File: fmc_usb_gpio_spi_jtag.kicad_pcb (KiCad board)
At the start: 2 copper layers, 76.5 x 69 mm, 146 parts, among them J1 SAMTEC_ASP-134604-01, J2 ACA-SPI-004-K02, J3 USB_C_Receptacle, J4 USB_C_Receptacle, J5 Conn_JTAG_20, J6 PM2.54-2x6, J7 Micro_SD_Card_Det2, J8 PM2.54-2x6, SW1 DSHP04TSGET, SW10 TL3342F160QG, SW2 TL3342F160QG, SW7 TL3342F160QG, SW8 TL3342F160QG, SW9 TL3342F160QG, U1 M24C02-FMN, U11 TXS02612RTWR, U12 TPD4E02B04DQA, U13 MT2492, U14 TXS02612RTWR, U15 TXS02612RTWR, U16 TXS02612RTWR, U17 TXS02612RTWR, U18 TPD4E02B04DQA, U19 TPD4E02B04DQA, U2 STUSB03EQR, U20 TPD4E02B04DQA, U21 AIP74LVC1T45GB236TR, U22 AIP74LVC1T45GB236TR, U23 AIP74LVC1T45GB236TR, U24 AIP74LVC1T45GB236TR, U25 MMC5603NJ, U26 TXS02612RTWR, U27 TXS02612RTWR, U3 CP2104, U4 TXS02612RTWR, U5 GX0011D

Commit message: *.*: add design rule file of PCB
Signed-off-by: Huang Rui <vowstar@gmail.com>
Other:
- copper layers 2 -> 4
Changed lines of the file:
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@@
   (layers
     (0 "F.Cu" signal)
+    (1 "In1.Cu" signal)
+    (2 "In2.Cu" signal)
     (31 "B.Cu" signal)
     (32 "B.Adhes" user "B.Adhesive")
@@
   )
   (setup
+    (stackup
+      (layer "F.SilkS" (type "Top Silk Screen"))
+      (layer "F.Paste" (type "Top Solder Paste"))
+      (layer "F.Mask" (type "Top Solder Mask") (thickness 0.01))
+      (layer "F.Cu" (type "copper") (thickness 0.035))
+      (layer "dielectric 1" (type "prepreg") (thickness 0.1) (material "FR4") (epsilon_r 4.5) (loss_tangent 0.02))
+      (layer "In1.Cu" (type "copper") (thickness 0.035))
+      (layer "dielectric 2" (type "core") (thickness 1.24) (material "FR4") (epsilon_r 4.5) (loss_tangent 0.02))
+      (layer "In2.Cu" (type "copper") (thickness 0.035))
+      (layer "dielectric 3" (type "prepreg") (thickness 0.1) (material "FR4") (epsilon_r 4.5) (loss_tangent 0.02))
+      (layer "B.Cu" (type "copper") (thickness 0.035))
+      (layer "B.Mask" (type "Bottom Solder Mask") (thickness 0.01))
+      (layer "B.Paste" (type "Bottom Solder Paste"))
+      (layer "B.SilkS" (type "Bottom Silk Screen"))
+      (copper_finish "None")
+      (dielectric_constraints no)
+    )
     (pad_to_mask_clearance 0)
     (aux_axis_origin 114.343703 64.989968)
@@
     (fp_arc (start 3.8 2.46) (mid 3.860908 2.157784) (end 4.03 1.9)
       (stroke (width 0.127) (type default)) (layer "F.SilkS"))
-    (fp_arc (start 4.03 -1.9) (mid 3.860909 -2.157783) (end 3.8 -2.46)
+    (fp_arc (start 4.03 -1.9) (mid 3.860928 -2.157792) (end 3.8 -2.46)
       (stroke (width 0.127) (type default)) (layer "F.SilkS"))
-    (fp_arc (start 4.37 -1.56) (mid 4.539091 -1.302217) (end 4.6 -1)
+    (fp_arc (start 4.37 -1.56) (mid 4.539072 -1.302208) (end 4.6 -1)
       (stroke (width 0.127) (type default)) (layer "F.SilkS"))
     (fp_arc (start 4.6 1) (mid 4.539092 1.302216) (end 4.37 1.56)
@@
     (fp_arc (start 3.8 2.46) (mid 3.860908 2.157784) (end 4.03 1.9)
       (stroke (width 0.1) (type default)) (layer "F.Fab"))
-    (fp_arc (start 4.03 -1.9) (mid 3.860909 -2.157783) (end 3.8 -2.46)
+    (fp_arc (start 4.03 -1.9) (mid 3.860928 -2.157792) (end 3.8 -2.46)
       (stroke (width 0.1) (type default)) (layer "F.Fab"))
-    (fp_arc (start 4.37 -1.56) (mid 4.539091 -1.302217) (end 4.6 -1)
+    (fp_arc (start 4.37 -1.56) (mid 4.539072 -1.302208) (end 4.6 -1)
       (stroke (width 0.1) (type default)) (layer "F.Fab"))
     (fp_arc (start 4.6 1) (mid 4.539092 1.302216) (end 4.37 1.56)
@@
     (fp_circle (center 26.5 6) (end 27 6)
       (stroke (width 0.1) (type solid)) (fill solid) (layer "B.Fab"))
-    (pad "" np_thru_hole circle locked (at -27.191 -3.048 270) (size 0.5 0.5) (drill 1.3) (layers "F&B.Cu" "*.Mask")
+    (pad "" np_thru_hole circle locked (at -27.191 -3.048 270) (size 0.5 0.5) (drill 1.3) (layers "*.Cu" "*.Mask")
       (solder_mask_margin 0.4))
     (pad "" np_thru_hole circle locked (at 27.191 0 270) (size 0.5 0.5) (drill 1.3) (layers "*.Cu" "*.Mask")

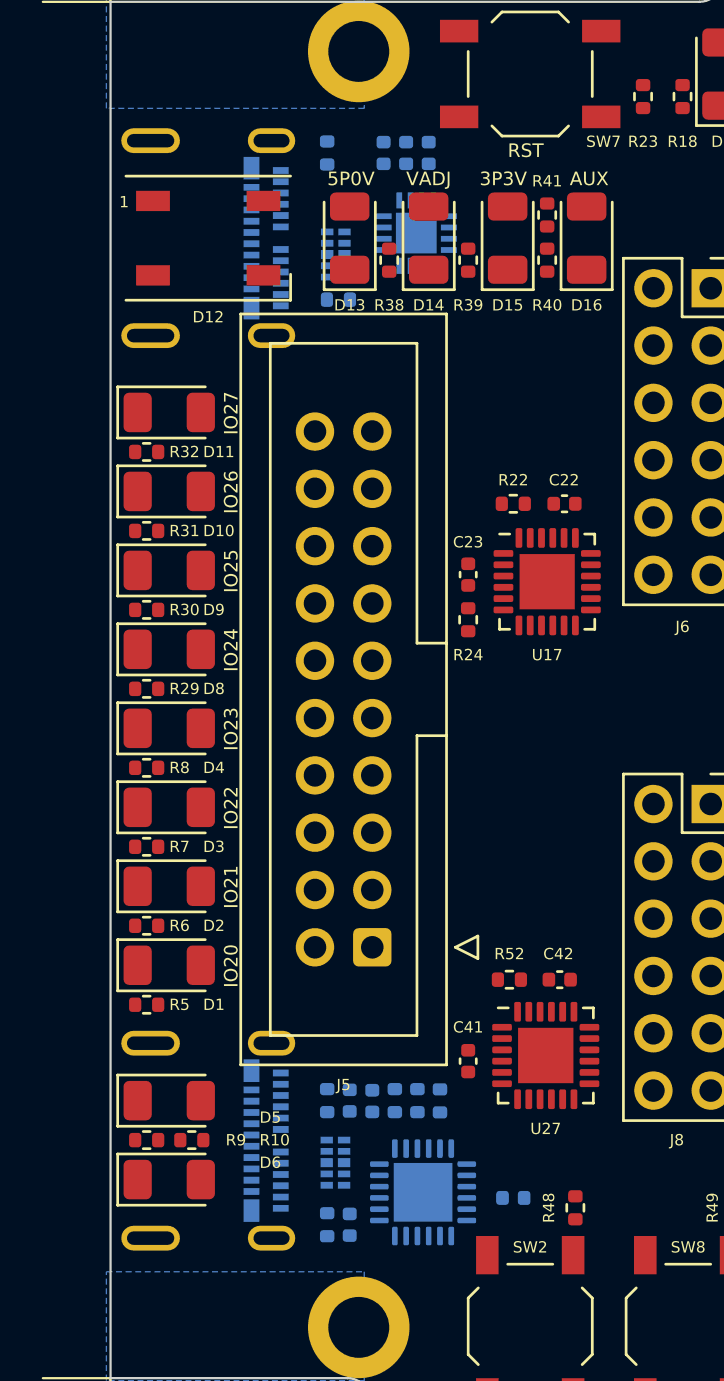
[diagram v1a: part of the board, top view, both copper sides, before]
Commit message: *.kicad_dru: fix design rule, add usb net class design rule
Signed-off-by: Huang Rui <vowstar@gmail.com>
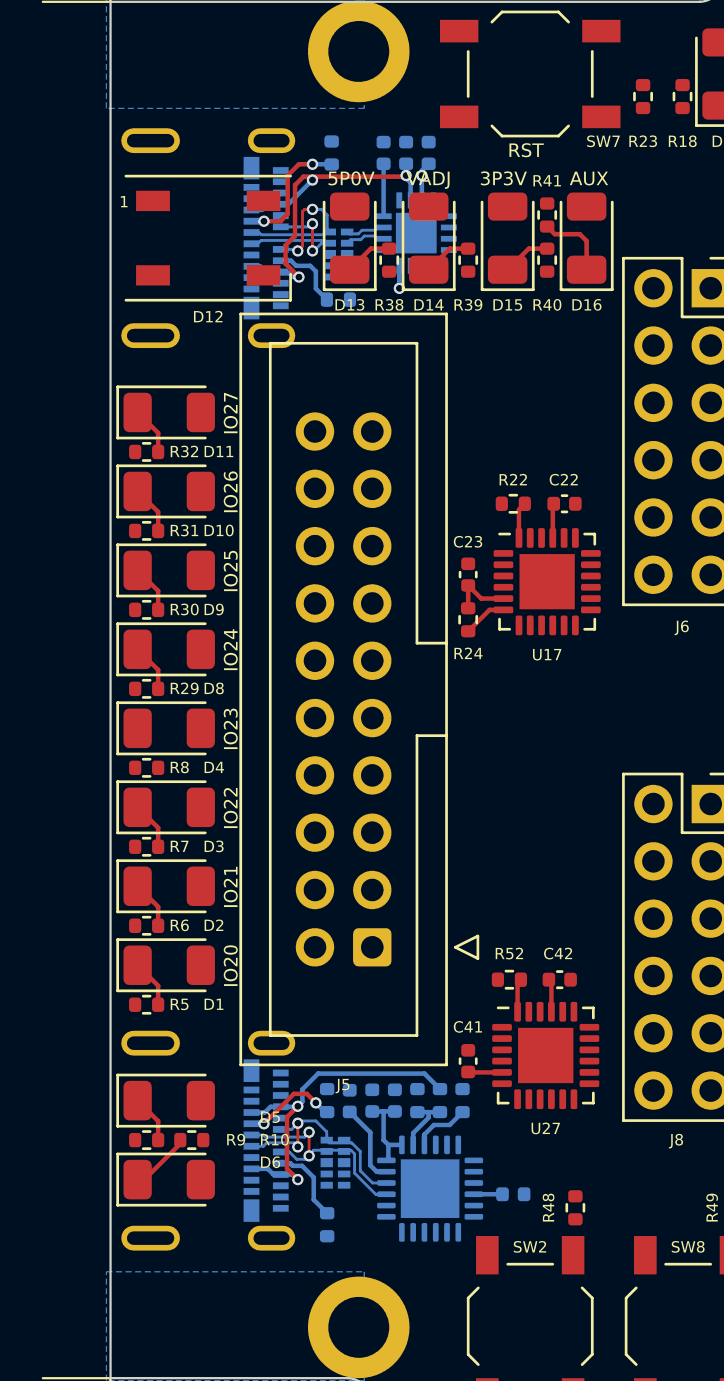
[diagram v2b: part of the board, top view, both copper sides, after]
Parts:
- moved C7 5.48 mm to (59.3, 114.0), turned to 90 degrees
- moved C6 1.00 mm to (61.3, 114.0)
- moved R35 1.00 mm to (64.3, 114.0)
- moved C8 1.00 mm to (60.3, 114.0)
- moved R36 1.00 mm to (63.3, 114.0)
- moved R37 1.00 mm to (62.3, 114.0)
- moved U3 0.35 mm to (62.9, 117.9)
- moved R2 0.20 mm to (58.5, 72.0)
- moved C9 0.16 mm to (66.6, 118.1)
- moved U18 0.11 mm to (58.8, 76.5)
- turned R24 to -90 degrees
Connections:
- net Net-(#FLG03-pwr) renamed /USB/USB_VBUS
- J4 pad A6: Net-(U12-IO4) -> /UART/D+
- J4 pad A7: Net-(U12-IO3) -> /UART/D-
- J4 pad B6: Net-(U12-IO4) -> /UART/D+
- J4 pad B7: Net-(U12-IO3) -> /UART/D-
- U12 pad 4: Net-(U12-IO3) -> /UART/D+
- U12 pad 5: Net-(U12-IO4) -> /UART/D-
- U12 pad 6: Net-(U12-IO4) -> /UART/D-
- U12 pad 7: Net-(U12-IO3) -> /UART/D+
- U3 pad 3: Net-(U12-IO4) -> /UART/D+
- U3 pad 4: Net-(U12-IO3) -> /UART/D-
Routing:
- net /USB/USB_VBUS: track 0.00 -> 16.8 mm, vias 0 -> 3
- net Net-(J4-VBUS-PadA4): track 0.00 -> 15.6 mm, vias 0 -> 2
- net /UART/D+: track 0.00 -> 10.0 mm, vias 0 -> 2
- net /USB/D+: track 0.00 -> 9.86 mm, vias 0 -> 2
- net /UART/D-: track 0.00 -> 9.62 mm, vias 0 -> 2
- net VADJ: track 1.97 -> 11.3 mm, vias 2 -> 4
- net /USB/D-: track 0.00 -> 8.83 mm, vias 0 -> 2
- net 3P3V: track 3.13 -> 11.3 mm
- net Net-(J3-CC2): track 0.00 -> 5.05 mm, vias 0 -> 2
- net Net-(J4-CC2): track 0.00 -> 3.68 mm, vias 0 -> 2
- net Net-(J4-CC1): track 0.00 -> 3.55 mm
- net Net-(D16-K): track 0.00 -> 3.29 mm
- net Net-(J3-CC1): track 0.00 -> 3.20 mm
- net Net-(U3-VBUS): track 0.00 -> 2.85 mm
- net Net-(D6-K): track 0.00 -> 2.71 mm
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
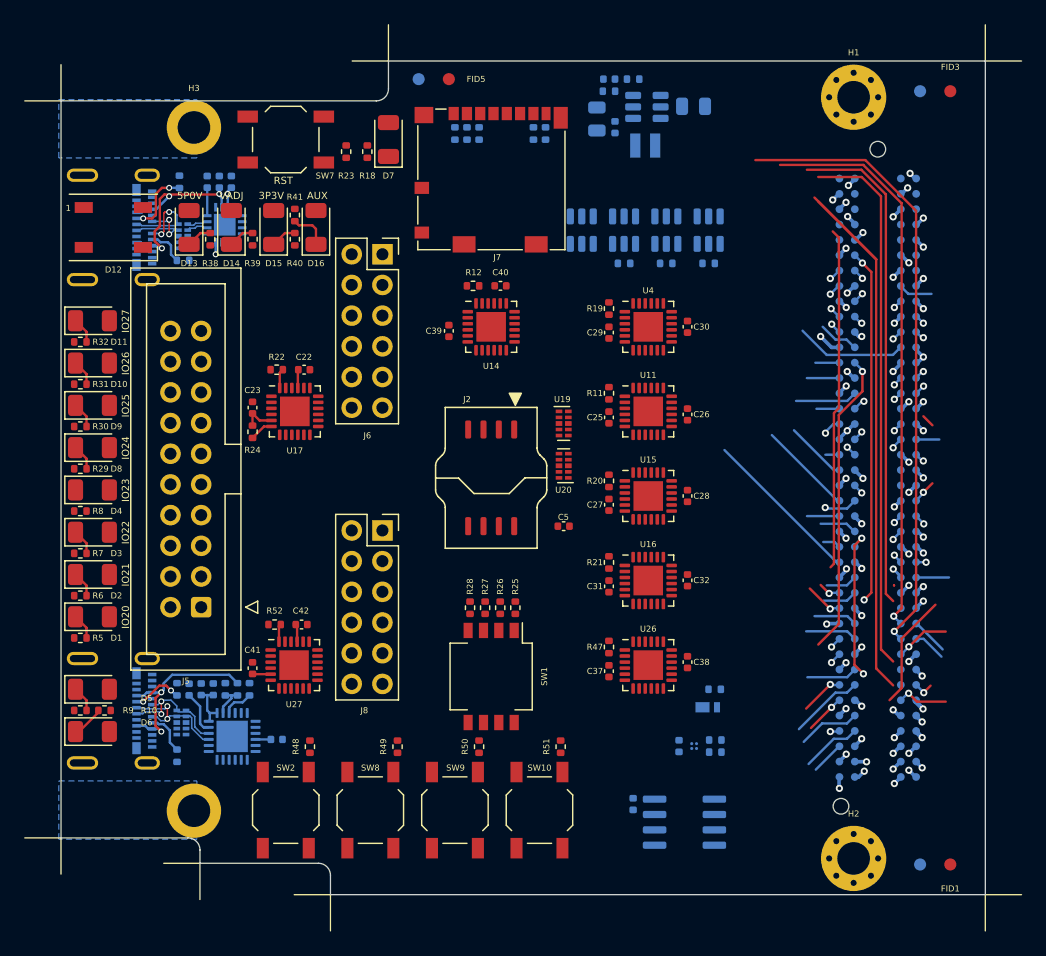
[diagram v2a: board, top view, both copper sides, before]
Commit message: *.*: adjust the level conversion chip and pre-layout the microsd
Signed-off-by: Huang Rui <vowstar@gmail.com>
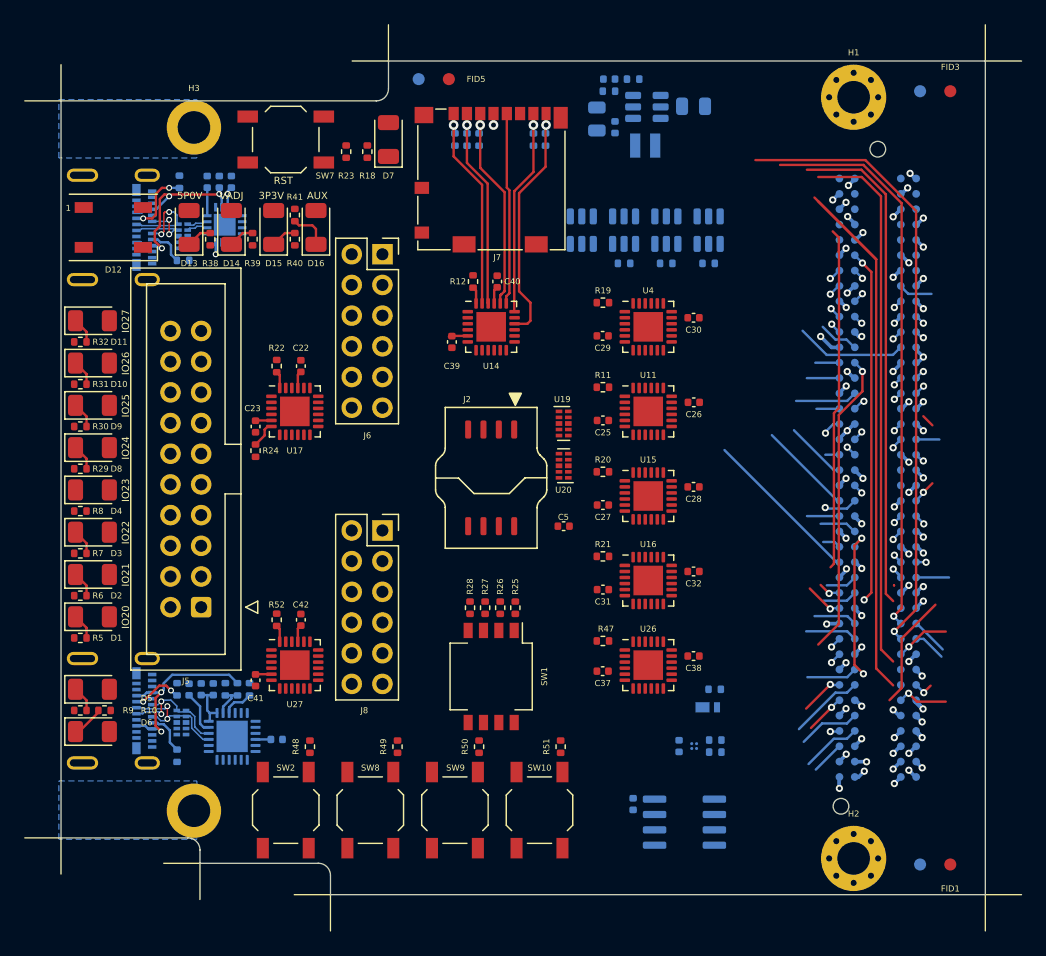
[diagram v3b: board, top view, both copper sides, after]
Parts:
- moved C23 1.58 mm to (64.8, 92.2), turned to -90 degrees
- moved R24 1.58 mm to (64.8, 94.2), turned to 90 degrees
- moved C26 1.13 mm to (101.1, 90.2), turned to 0 degrees
- moved C41 1.03 mm to (64.8, 113.2), turned to -90 degrees
- moved C39 0.94 mm to (81.1, 85.2), turned to -90 degrees
- moved C28 0.90 mm to (101.1, 97.2), turned to 0 degrees
- moved C30 0.90 mm to (101.1, 83.2), turned to 0 degrees
- moved R20 0.90 mm to (93.6, 96.0), turned to 0 degrees
- moved C32 0.88 mm to (101.1, 104.2), turned to 0 degrees
- moved C38 0.71 mm to (101.1, 111.2), turned to 0 degrees
- moved R11 0.71 mm to (93.6, 89.0), turned to 0 degrees
- moved R21 0.71 mm to (93.6, 103.0), turned to 0 degrees
- moved R47 0.71 mm to (93.6, 110.0), turned to 0 degrees
- moved R19 0.70 mm to (93.6, 82.0), turned to 0 degrees
- moved C29 0.59 mm to (93.6, 84.7), turned to 180 degrees
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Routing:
- net /SDIO/SD_DAT1: track 0.00 -> 20.6 mm, vias 0 -> 1
- net /SDIO/SD_DAT0: track 0.00 -> 17.8 mm, vias 0 -> 1
- net /SDIO/SD_CMD: track 0.00 -> 17.4 mm, vias 0 -> 1
- net /SDIO/SD_DAT2: track 0.00 -> 17.4 mm, vias 0 -> 1
- net /SDIO/SD_DAT3: track 0.00 -> 17.1 mm, vias 0 -> 1
- net /SDIO/SD_CLK: track 0.00 -> 15.9 mm
- net Net-(U14-SEL): track 0.00 -> 1.41 mm
- net VADJ: track 11.3 -> 12.5 mm
- net 3P3V: track 11.3 -> 12.2 mm, vias 4 -> 5

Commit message: *.*: finish flash and sdio layout
Signed-off-by: Huang Rui <vowstar@gmail.com>
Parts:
- C5, U19, U20: moved to B.Cu
- moved R53 13.7 mm to (97.0, 126.4), turned to -90 degrees
- moved U5 12.6 mm to (95.5, 126.1), turned to -90 degrees
- moved R43 11.5 mm to (93.0, 124.1), turned to -90 degrees
- moved C36 10.5 mm to (93.5, 127.1), turned to 0 degrees
- moved U25 10.4 mm to (93.5, 125.8), turned to 90 degrees
- moved R42 10.1 mm to (94.0, 124.1), turned to -90 degrees
- moved U20 7.14 mm to (83.5, 97.6), turned to 90 degrees
- moved U19 6.79 mm to (86.5, 97.6), turned to 90 degrees
- moved C5 3.08 mm to (87.3, 100.7), turned to 90 degrees
- moved C1 1.21 mm to (97.3, 123.2)
- moved U1 1.21 mm to (101.5, 124.7)
- moved C9 0.50 mm to (67.1, 118.1)
- moved U3 0.50 mm to (63.4, 117.9)
- moved C23 0.15 mm to (64.8, 92.4)
- moved R24 0.15 mm to (64.8, 94.4)
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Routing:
- net Net-(J1B-d30): track 98.1 -> 1.63 mm
- net /FMC/SDIO.DAT2: track 3.57 -> 77.3 mm
- net /FMC/SDIO.CMD: track 0.74 -> 72.9 mm
- net /FMC/SDIO.DAT3: track 3.27 -> 75.2 mm
- net /FMC/SDIO.DAT0: track 0.95 -> 70.6 mm
- net /FMC/SDIO.DAT1: track 0.96 -> 68.9 mm
- net /FMC/SDIO.CLK: track 2.72 -> 66.0 mm, vias 0 -> 1
- net /FMC/SPI_FLASH.~{WP}: track 1.51 -> 60.0 mm, vias 0 -> 1
- net /FMC/SPI_FLASH.DO: track 2.69 -> 60.2 mm, vias 0 -> 1
- net /FMC/SPI_FLASH.CLK: track 1.87 -> 58.6 mm
- net /FMC/SPI_FLASH.DI: track 3.18 -> 59.2 mm
- net /FMC/SPI_FLASH.~{CS}: track 7.85 -> 60.2 mm, vias 0 -> 1
- net unconnected-(J1B-d34-PadD34): track 49.9 -> 0.00 mm
- net /FMC/SPI_FLASH.~{HOLD}: track 13.4 -> 59.7 mm, vias 0 -> 1
- net unconnected-(J1B-d33-PadD33): track 44.8 -> 0.00 mm
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
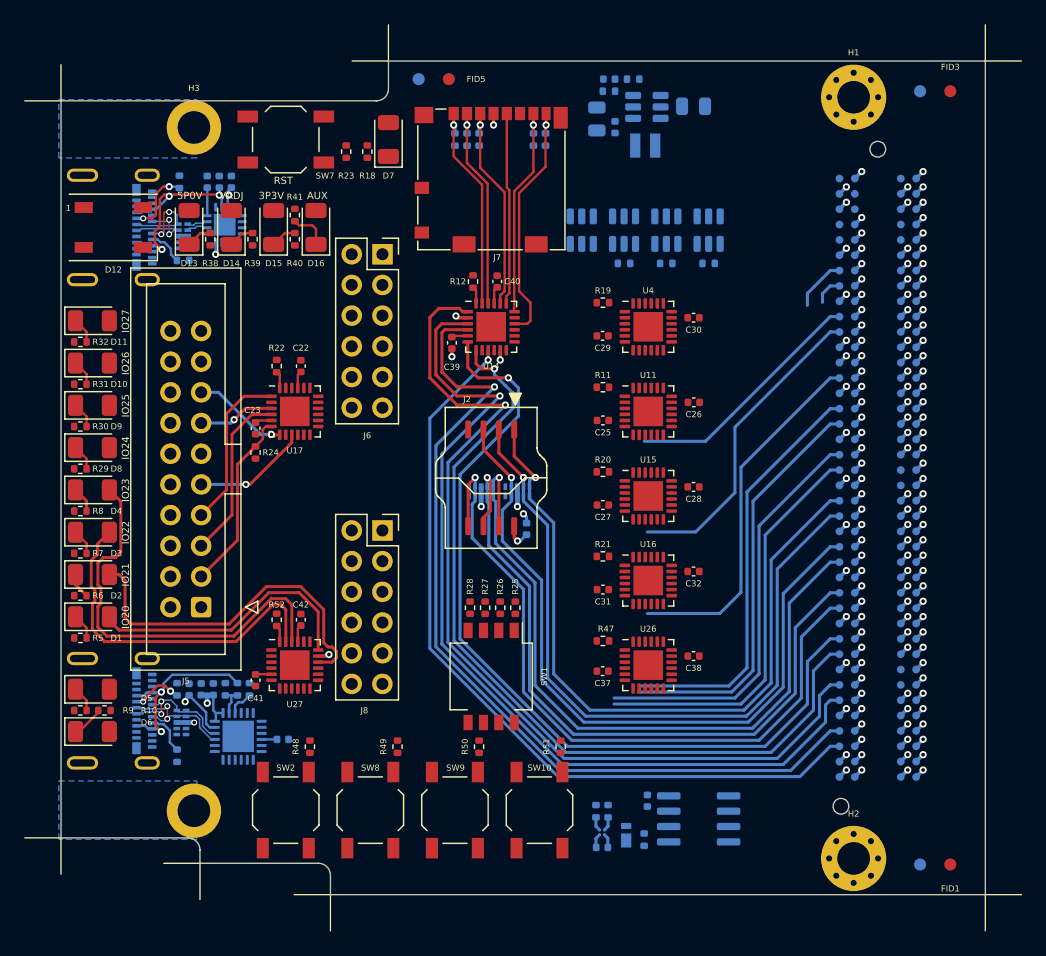
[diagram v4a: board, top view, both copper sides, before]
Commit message: *.kicad_pcb: adjust levelshifter layout
Signed-off-by: Huang Rui <vowstar@gmail.com>
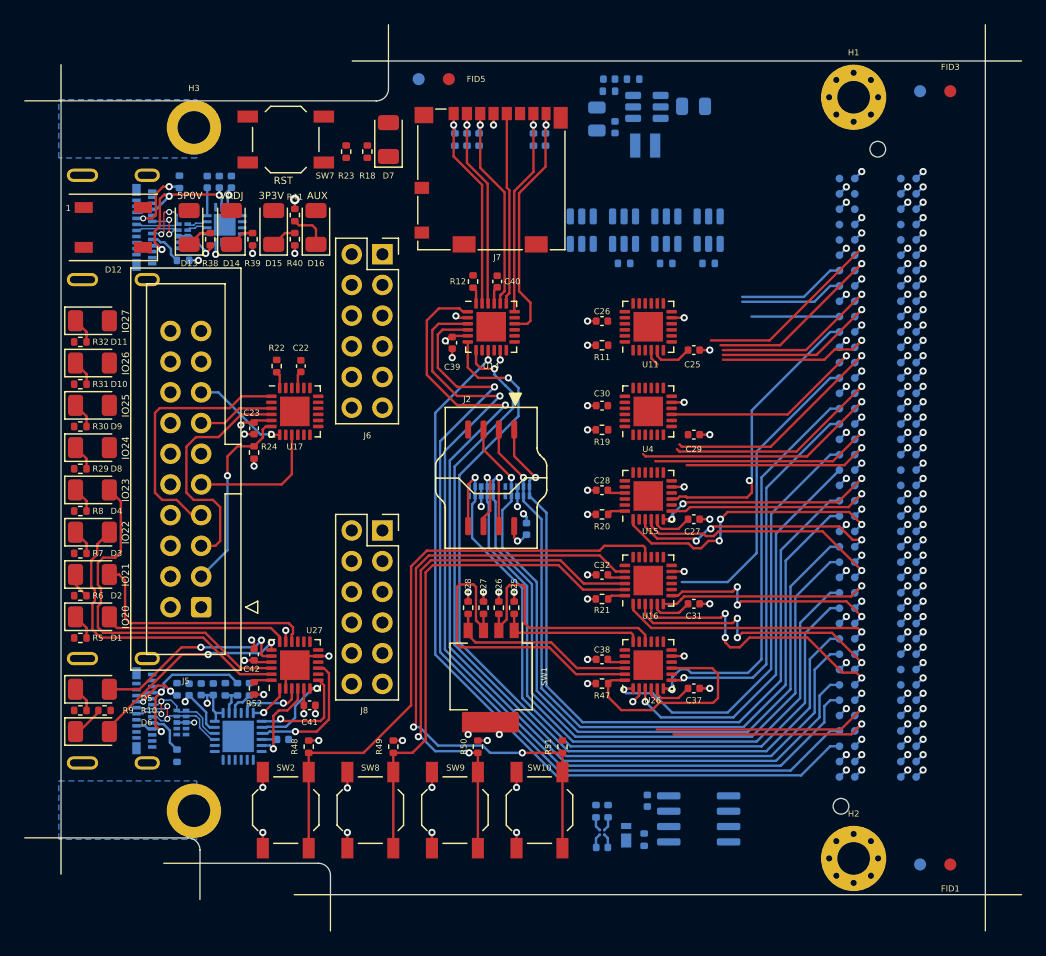
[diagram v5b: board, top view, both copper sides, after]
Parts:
- moved C29 11.1 mm to (101.1, 92.9), turned to 0 degrees
- moved R19 10.5 mm to (93.5, 92.5)
- moved C30 10.5 mm to (93.5, 90.5), turned to 180 degrees
- moved C26 10.1 mm to (93.5, 83.5), turned to 180 degrees
- moved C25 9.52 mm to (101.1, 85.9), turned to 0 degrees
- moved C37 7.68 mm to (101.1, 113.9), turned to 0 degrees
- moved C27 7.62 mm to (101.1, 99.9), turned to 0 degrees
- moved C31 7.62 mm to (101.1, 106.9), turned to 0 degrees
- moved C28 7.58 mm to (93.5, 97.5), turned to 180 degrees
- moved C32 7.58 mm to (93.5, 104.5), turned to 180 degrees
- moved C38 7.58 mm to (93.5, 111.5), turned to 180 degrees
- moved U11 7.00 mm to (97.3, 84.0), turned to 90 degrees
- moved U4 7.00 mm to (97.3, 91.0), turned to 90 degrees
- moved R52 5.98 mm to (64.7, 113.9), turned to 90 degrees
- moved C41 4.93 mm to (69.3, 115.3), turned to 0 degrees
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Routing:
- net /GPIO/HVGPIO19: track 0.00 -> 52.4 mm, vias 0 -> 2
- net /GPIO/HVGPIO16: track 0.00 -> 50.4 mm
- net /GPIO/HVGPIO18: track 0.00 -> 45.3 mm, vias 0 -> 2
- net GND: track 60.4 -> 104.4 mm, vias 69 -> 110
- net /GPIO/HVGPIO17: track 0.00 -> 42.4 mm
- net /GPIO/HVGPIO30: track 0.00 -> 26.6 mm
- net /FMC/GPIO20: track 0.81 -> 25.5 mm, vias 1 -> 2
- net /FMC/GPIO21: track 0.81 -> 25.5 mm, vias 1 -> 2
- net /FMC/GPIO12: track 0.81 -> 23.7 mm, vias 1 -> 3
- net /FMC/GPIO19: track 0.81 -> 23.6 mm, vias 1 -> 3
- net /FMC/GPIO18: track 0.81 -> 22.9 mm, vias 1 -> 3
- net /GPIO/HVGPIO29: track 0.00 -> 20.8 mm
- net /FMC/GPIO17: track 0.81 -> 21.0 mm
- net /FMC/GPIO7: track 0.81 -> 20.9 mm
- net Net-(U26-CLKA): track 0.00 -> 20.0 mm
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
